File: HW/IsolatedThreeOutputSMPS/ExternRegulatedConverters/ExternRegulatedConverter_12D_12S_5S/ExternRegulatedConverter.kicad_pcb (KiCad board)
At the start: 2 copper layers, 71.1 x 49.5 mm, 18 parts, among them J1 Conn_01x02, J2 Conn_01x05, U1 RS6-1212D, U2 LM7805_TO220, U3 LM7812_TO220, U4 LM7912_TO220

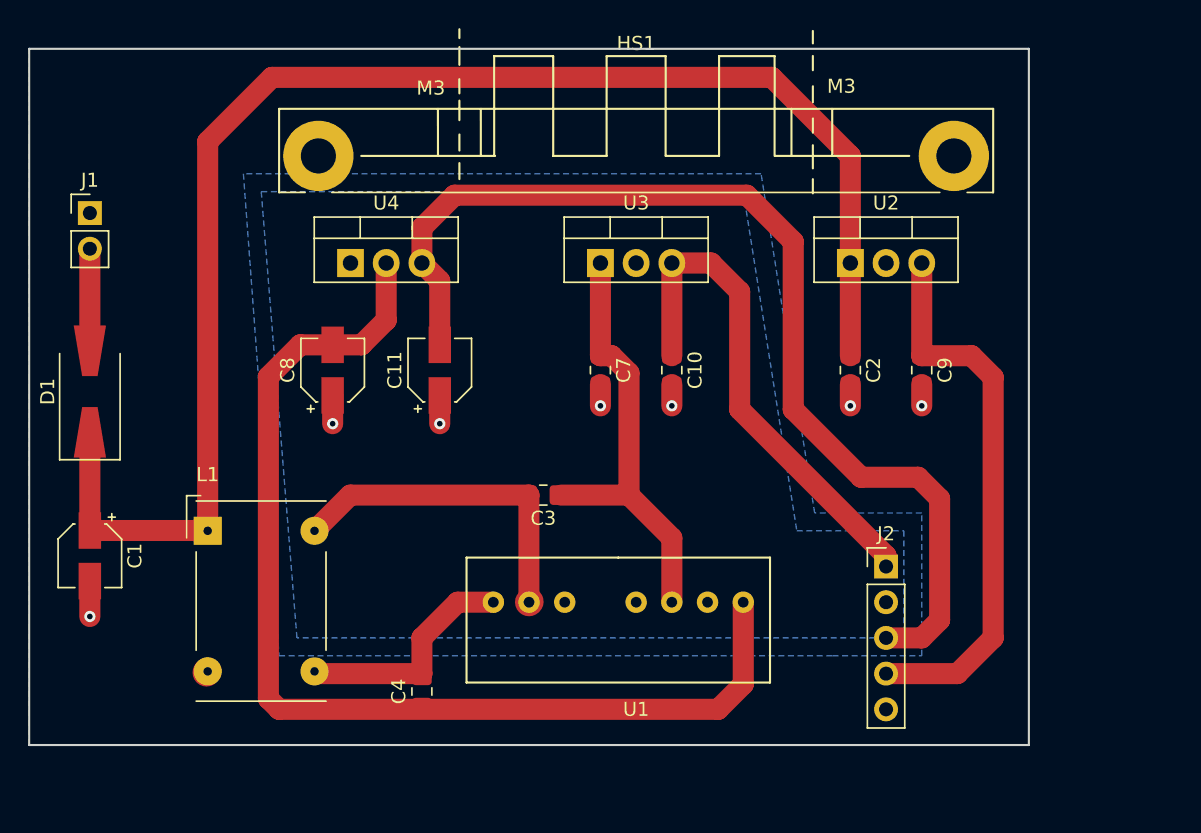
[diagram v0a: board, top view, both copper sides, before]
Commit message: updated hw
- finished layout for power supply
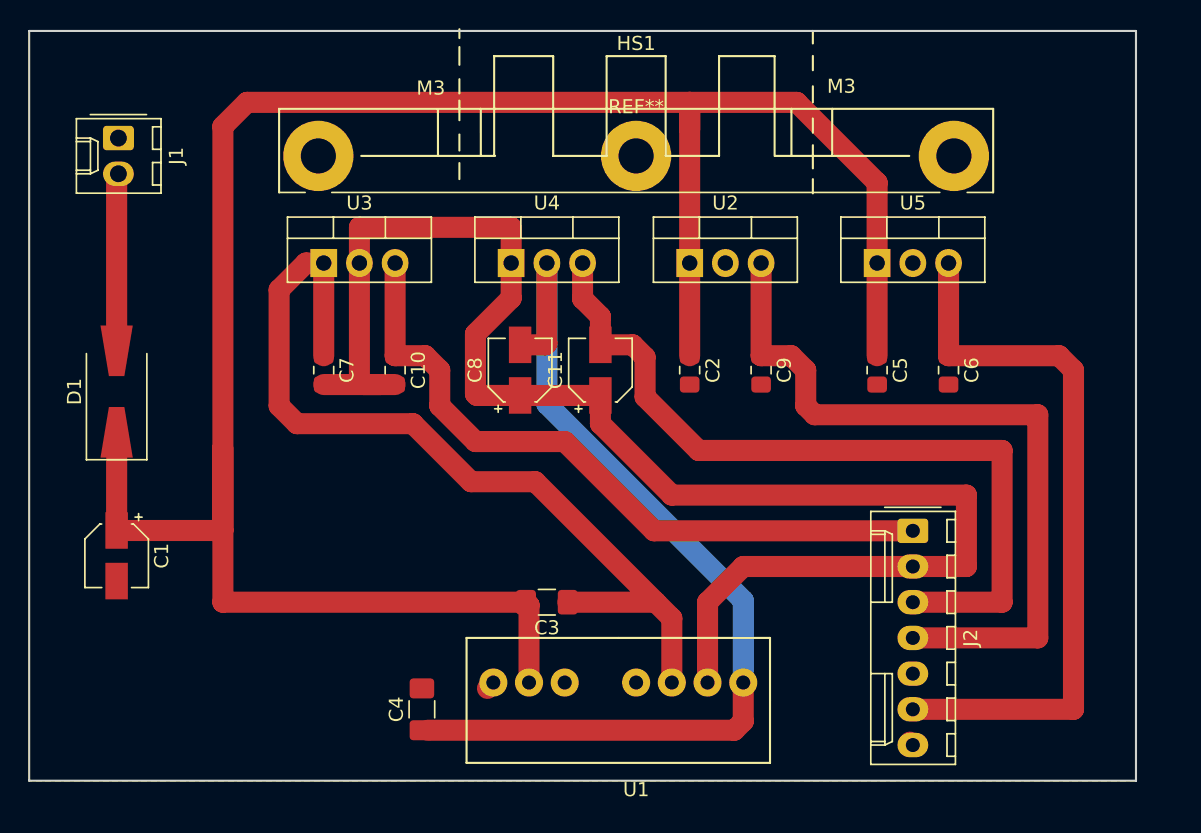
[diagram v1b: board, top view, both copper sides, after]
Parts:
- removed L1: 10mH, Inductor_THT:Choke_Schaffner_RN204-04-9.0x14.0mm
- added C5: 330nF, Capacitor_SMD:C_0805_2012Metric_Pad1.15x1.40mm_HandSolder, F.Cu at (151.8, 90.2)
- added C6: 100nF, Capacitor_SMD:C_0805_2012Metric_Pad1.15x1.40mm_HandSolder, F.Cu at (156.8, 90.2)
- added REF**: MountingHole_2.5mm_Pad, MountingHole:MountingHole_2.5mm_Pad, F.Cu at (134.6, 74.9)
- added U5: LM7812_TO220, Package_TO_SOT_THT:TO-220-3_Vertical, F.Cu at (151.8, 82.5)
- C11: value 1uF -> 10uF
- C2: value 200nF -> 330nF
- C3, C4: footprint Capacitor_SMD:C_0805_2012Metric_Pad1.15x1.40mm_HandSolder -> Capacitor_SMD:C_1206_3216Metric_Pad1.42x1.75mm_HandSolder
- C7: value 220nF -> 330nF
- C8: value 2.2uF -> 10uF
- J1: value Conn_01x02 -> 15VDC; footprint Connector_PinHeader_2.54mm:PinHeader_1x02_P2.54mm_Vertical -> Connector_Molex:Molex_KK-254_AE-6410-02A_1x02_P2.54mm_Vertical
- J2: value Conn_01x05 -> Conn_01x07; footprint Connector_PinHeader_2.54mm:PinHeader_1x05_P2.54mm_Vertical -> Connector_Molex:Molex_KK-254_AE-6410-07A_1x07_P2.54mm_Vertical
- moved C7 19.7 mm to (112.4, 90.2)
- moved U3 19.7 mm to (112.4, 82.5)
- moved C10 19.7 mm to (117.5, 90.2)
- moved C8 13.3 mm to (126.4, 90.2)
- moved C11 11.4 mm to (132.1, 90.2)
- moved C2 11.4 mm to (138.4, 90.2)
- moved C9 11.4 mm to (143.5, 90.2)
- moved U2 11.4 mm to (138.4, 82.5)
- moved U4 11.4 mm to (125.7, 82.5)
- moved C3 7.62 mm to (128.3, 106.7)
- moved U1 5.71 mm to (132.1, 112.4)
- moved J1 5.71 mm to (97.8, 73.7), turned to 270 degrees
- moved J2 3.18 mm to (154.3, 101.6), turned to 270 degrees
- moved C1 1.91 mm to (97.7, 103.4)
- moved D1 1.91 mm to (97.7, 91.7)
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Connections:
- C1 pad 1: VDD -> +15V
- C2 pad 1: VDD -> +15V
- C3 pad 2: Net-(C3-Pad2) -> +15V
- C4 pad 2: Net-(C4-Pad2) -> GNDA
- D1 pad 1: VDD -> +15V
- U1 pad 1: Net-(C4-Pad2) -> GNDA
- U1 pad 2: Net-(C3-Pad2) -> +15V
- U2 pad 1: VDD -> +15V
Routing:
- net +15V: track 0.00 -> 163.5 mm
- net VDD: track 106.9 -> 0.00 mm
- net VCOM: track 7.05 -> 110.7 mm, vias 4 -> 0
- net +12P: track 0.00 -> 51.5 mm
- net Net-(C3-Pad1): track 31.5 -> 63.8 mm
- net Net-(C3-Pad2): track 24.0 -> 0.00 mm
- net -12V: track 75.5 -> 56.8 mm
- net Net-(C4-Pad2): track 16.4 -> 0.00 mm
- net +5V: track 39.5 -> 54.3 mm
- net +12V: track 36.1 -> 50.1 mm
- net Net-(C4-Pad1): track 77.7 -> 68.8 mm
- net Net-(D1-Pad2): track 7.26 -> 12.6 mm
- net GNDA: track 5.66 -> 0.88 mm, vias 3 -> 0
- added copper zone on F.Cu, net GNDA
- removed copper zone on B.Cu, net GNDA
- removed copper zone on B.Cu, net VCOM
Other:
- board size 71.1 x 49.5 mm -> 78.7 x 53.3 mm

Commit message: updated HW
- ExternRegulatedConverter_12D_12S_5S layout optimised for etching
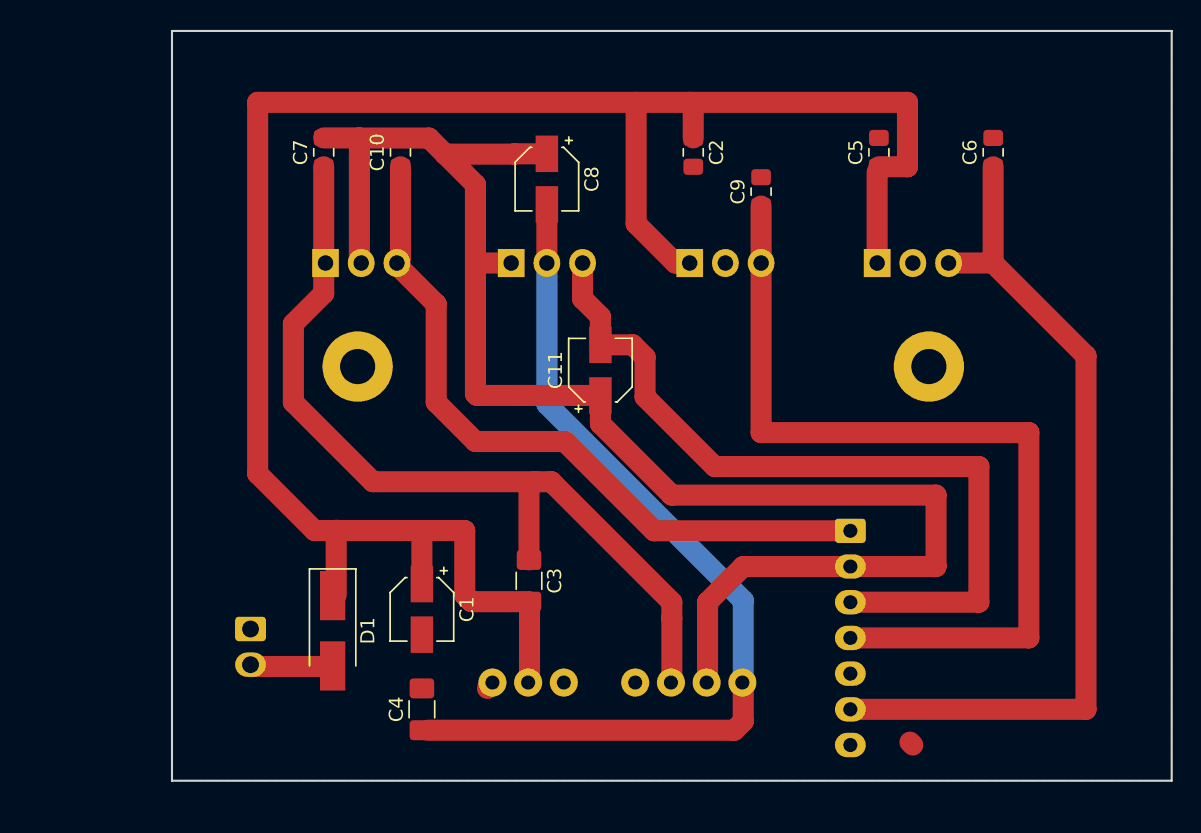
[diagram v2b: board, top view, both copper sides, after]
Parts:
- removed REF**: MountingHole_2.5mm_Pad, MountingHole:MountingHole_2.5mm_Pad
- C1: value 10uF -> 2.2uF
- C3: value 47p -> 33p
- C4: value 100p -> 220p
- D1: footprint Diode_SMD:D_SMA-SMB_Universal_Handsoldering -> Diode_SMD:D_SMA_Handsoldering
- HS1, J1, J2, U1, U2, U3, U4, U5: moved to B.Cu
- moved J1 36.2 mm to (107.2, 108.6)
- moved D1 22.9 mm to (113.0, 108.7), turned to 270 degrees
- moved C1 22.0 mm to (119.4, 107.2)
- moved C6 15.8 mm to (160.0, 74.7), turned to 90 degrees
- moved C10 15.5 mm to (117.9, 74.7), turned to 90 degrees
- moved C2 15.5 mm to (138.7, 74.7)
- moved C5 15.5 mm to (151.9, 74.7), turned to 90 degrees
- moved C7 15.5 mm to (112.4, 74.7), turned to 90 degrees
- moved HS1 15.0 mm to (135.1, 89.9)
- moved C8 13.7 mm to (128.3, 76.6), turned to 270 degrees
- moved C9 12.7 mm to (143.5, 77.5), turned to 90 degrees
- moved J2 4.44 mm to (149.9, 101.6)
- moved C3 1.98 mm to (127.0, 105.2), turned to 270 degrees
- moved U3 0.13 mm to (112.5, 82.5)
- moved U1 0.06 mm to (132.0, 112.4)
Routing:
- net +15V: track 163.5 -> 142.0 mm
- net +12P: track 51.5 -> 61.3 mm
- net +5V: track 54.3 -> 62.5 mm
- net Net-(D1-Pad2): track 12.6 -> 5.91 mm
- net Net-(C4-Pad1): track 68.8 -> 65.3 mm
- net Net-(C3-Pad1): track 63.8 -> 61.9 mm
- net +12V: track 50.1 -> 51.4 mm
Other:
- board size 78.7 x 53.3 mm -> 71.1 x 53.3 mm
